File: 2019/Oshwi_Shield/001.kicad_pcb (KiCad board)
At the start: 2 copper layers, 74.7 x 96.8 mm, 1 part

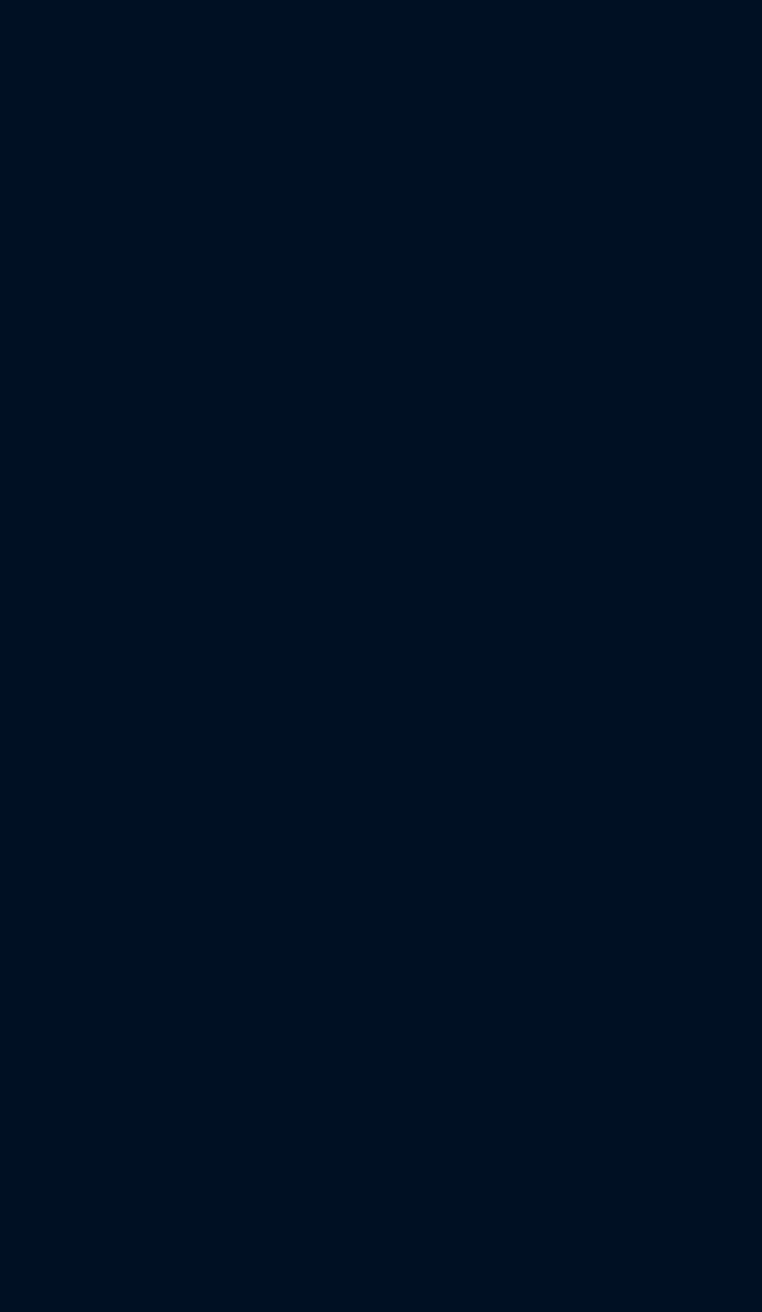
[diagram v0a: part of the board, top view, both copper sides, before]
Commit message: Add Info TFT
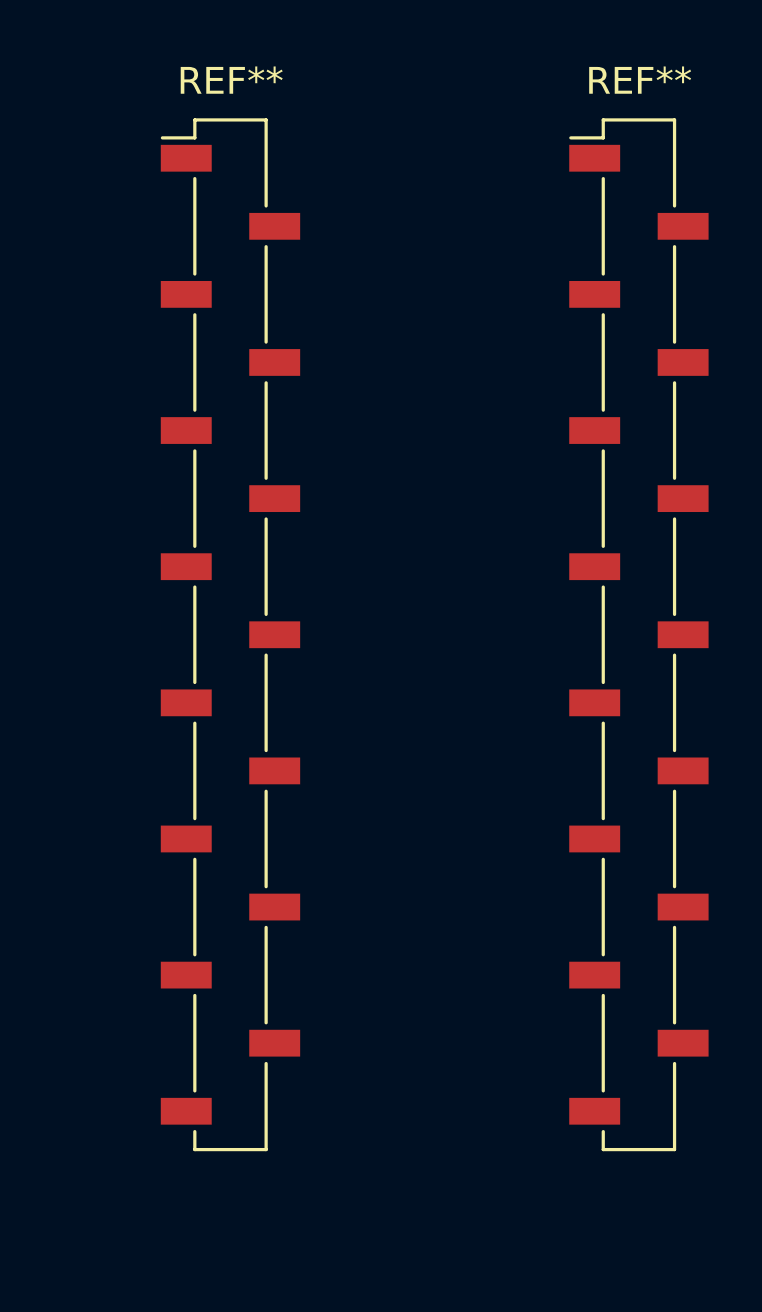
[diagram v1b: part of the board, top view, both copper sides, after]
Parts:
- added REF**: PinSocket_1x15_P2.54mm_Vertical_SMD_Pin1Left, Connector_PinSocket_2.54mm:PinSocket_1x15_P2.54mm_Vertical_SMD_Pin1Left, F.Cu at (193.0, 69.8)
- added REF**: PinSocket_1x15_P2.54mm_Vertical_SMD_Pin1Left, Connector_PinSocket_2.54mm:PinSocket_1x15_P2.54mm_Vertical_SMD_Pin1Left, F.Cu at (177.8, 69.8)
